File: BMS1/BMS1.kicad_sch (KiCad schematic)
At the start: 54 parts, among them J1 Conn_01x02, J2 Conn_01x02, J3 Conn_01x02, Q2 DXT5551P5-13_DIO, Q3 DXT5551P5-13_DIO, T1 ESMIT-4180_C, U1 ADG728, U10 LTC6812-1, U2 ADG728, U3 ADG728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

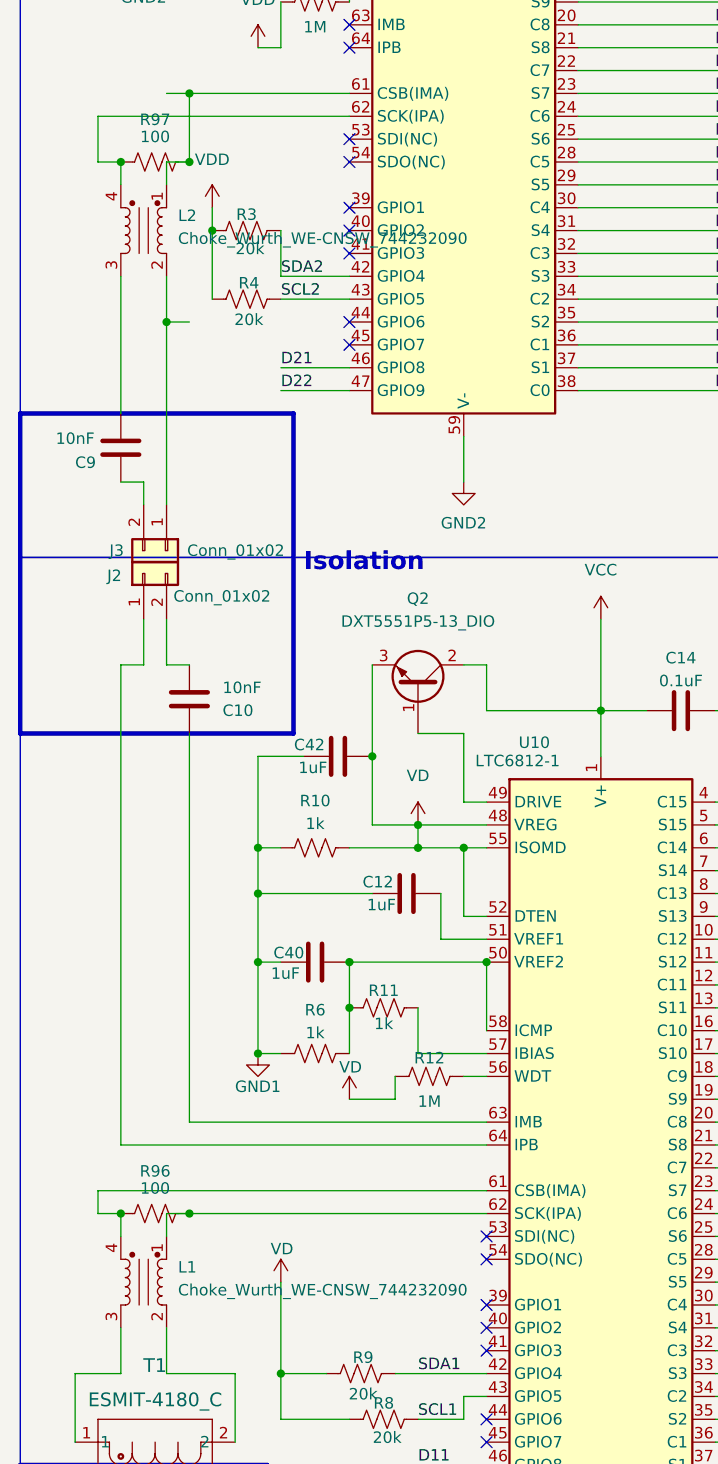
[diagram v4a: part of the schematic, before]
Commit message: updated choke symbol and footprint
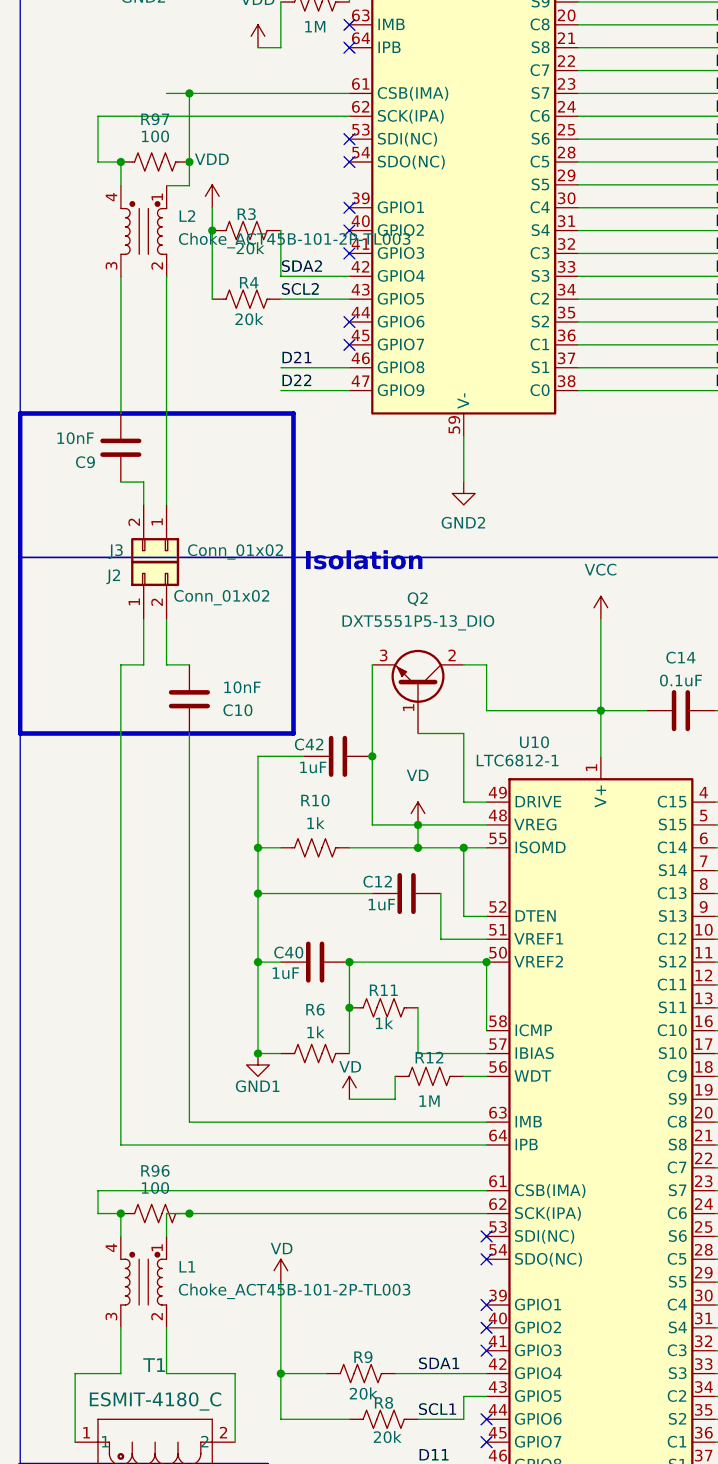
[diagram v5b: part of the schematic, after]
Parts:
- L1, L2: value Choke_Wurth_WE-CNSW_744232090 -> Choke_ACT45B-101-2P-TL003; footprint Inductor_SMD:L_CommonMode_Wurth_WE-CNSW-1206 -> AERO_Footprints:ACT45B-101-2P-TL003_TDK_new
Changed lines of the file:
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@@
 	)
 	(junction
-		(at 27.94 88.9)
-		(diameter 0)
-		(color 0 0 0 0)
-	)
-	(junction
 		(at 60.96 165.1)
 		(diameter 0)
@@
 	)
 	(junction
-		(at 33.02 106.68)
+		(at 68.58 177.8)
 		(diameter 0)
 		(color 0 0 0 0)
 	)
 	(junction
-		(at 68.58 177.8)
+		(at 231.14 43.18)
 		(diameter 0)
 		(color 0 0 0 0)
 	)
 	(junction
-		(at 231.14 43.18)
+		(at 27.94 88.9)
 		(diameter 0)
 		(color 0 0 0 0)
@@
 	(wire
 		(pts
-			(xy 33.02 101.6) (xy 33.02 106.68)
+			(xy 27.9516 116.84) (xy 27.94 116.84)
 		)
 		(stroke
@@
 	(wire
 		(pts
+			(xy 33.02 127) (xy 33.02 101.6945)
+		)
+		(stroke
+			(width 0)
+			(type default)
+		)
+	)
+	(wire
+		(pts
 			(xy 33.02 205.74) (xy 35.56 205.74)
 		)
@@
 	(wire
 		(pts
+			(xy 35.56 91.5345) (xy 33.0316 91.5345)
+		)
+		(stroke
+			(width 0)
+			(type default)
+		)
+	)
+	(wire
+		(pts
 			(xy 53.34 182.88) (xy 53.34 187.96)
 		)
@@
 		)
 	)
-	(wire
-		(pts
-			(xy 33.02 106.68) (xy 33.02 127)
-		)
-		(stroke
-			(width 0)
-			(type default)
-		)
-	)
 	(bus
 		(pts
@@
 	(wire
 		(pts
-			(xy 27.94 101.6) (xy 27.94 116.84)
-		)
-		(stroke
-			(width 0)
-			(type default)
-		)
-	)
-	(wire
-		(pts
 			(xy 27.94 198.12) (xy 68.58 198.12)
 		)
@@
 	(wire
 		(pts
-			(xy 226.06 167.64) (xy 226.06 170.18)
+			(xy 27.94 88.9) (xy 27.9516 88.9)
 		)
 		(stroke
@@
 	(wire
 		(pts
-			(xy 78.74 111.76) (xy 106.68 111.76)
+			(xy 226.06 167.64) (xy 226.06 170.18)
 		)
 		(stroke
@@
 	(wire
 		(pts
-			(xy 269.24 238.76) (xy 274.32 238.76)
+			(xy 78.74 111.76) (xy 106.68 111.76)
 		)
 		(stroke
@@
 	(wire
 		(pts
-			(xy 43.18 170.18) (xy 43.18 177.8)
+			(xy 269.24 238.76) (xy 274.32 238.76)
 		)
 		(stroke
@@
 	(wire
 		(pts
-			(xy 93.98 172.72) (xy 124.46 172.72)
+			(xy 43.18 170.18) (xy 43.18 177.8)
 		)
 		(stroke
@@
 	(wire
 		(pts
-			(xy 294.64 187.96) (xy 299.72 187.96)
+			(xy 93.98 172.72) (xy 124.46 172.72)
 		)
 		(stroke
@@
 	(wire
 		(pts
-			(xy 241.3 213.36) (xy 241.3 210.82)
+			(xy 294.64 187.96) (xy 299.72 187.96)
 		)
 		(stroke
@@
 	(wire
 		(pts
-			(xy 68.58 144.78) (xy 68.58 149.86)
+			(xy 241.3 213.36) (xy 241.3 210.82)
 		)
 		(stroke
@@
 	(wire
 		(pts
-			(xy 33.02 88.9) (xy 35.56 88.9)
+			(xy 68.58 144.78) (xy 68.58 149.86)
 		)
 		(stroke
@@
 	(wire
 		(pts
+			(xy 35.56 88.9) (xy 35.56 91.5345)
+		)
+		(stroke
+			(width 0)
+			(type default)
+		)
+	)
+	(wire
+		(pts
 			(xy 261.62 35.56) (xy 261.62 45.72)
 		)
@@
 	(wire
 		(pts
+			(xy 27.9516 101.6945) (xy 27.9516 116.84)
+		)
+		(stroke
+			(width 0)
+			(type default)
+		)
+	)
+	(wire
+		(pts
 			(xy 226.06 162.56) (xy 231.14 162.56)
 		)
@@
 	(wire
 		(pts
+			(xy 27.9516 88.9) (xy 27.9516 91.5345)
+		)
+		(stroke
+			(width 0)
+			(type default)
+		)
+	)
+	(wire
+		(pts
 			(xy 213.36 220.98) (xy 213.36 223.52)
 		)
@@
 		)
 	)
-	(wire
-		(pts
-			(xy 27.94 91.44) (xy 27.94 88.9)
-		)
-		(stroke
-			(width 0)
-			(type default)
-		)
-	)
 	(bus
 		(pts
@@
 	(wire
 		(pts
-			(xy 33.02 91.44) (xy 33.02 88.9)
+			(xy 33.02 101.6945) (xy 33.0316 101.6945)
 		)
 		(stroke
@@
 	(wire
 		(pts
-			(xy 33.02 106.68) (xy 35.56 106.68)
-		)
-		(stroke
-			(width 0)
-			(type default)
-		)
-	)
-	(wire
-		(pts
 			(xy 223.52 185.42) (xy 231.14 185.42)
 		)
@@
 	)
 	(symbol
+		(lib_name "Choke_Wurth_WE-CNSW_744232090_1")
+		(lib_id "Filter:Choke_Wurth_WE-CNSW_744232090")
+		(at 30.4916 96.6145 270)
+		(unit 1)
+		(exclude_from_sim no)
+		(in_bom yes)
+		(on_board yes)
+		(dnp no)
+		(fields_autoplaced yes)
+		(property "Reference" "L2"
+			(at 34.3016 94.9634 90)
+			(effects
+				(font
+					(size 1.27 1.27)
+				)
+				(justify left)
+			)
+		)
+		(property "Value" "Choke_ACT45B-101-2P-TL003"
+			(at 34.3016 97.5034 90)
+			(effects
+				(font
+					(size 1.27 1.27)
+				)
+				(justify left)
+			)
+		)
+		(property "Footprint" "AERO_Footprints:ACT45B-101-2P-TL003_TDK_new"
+			(at 20.3316 96.6145 0)
+			(effects
+				(font
+					(size 1.27 1.27)
+				)
+				(hide yes)
+			)
+		)
+		(property "Datasheet" "https://www.we-online.com/components/products/datasheet/744232090.pdf"
+			(at 22.8716 96.6145 0)
+			(effects
+				(font
+					(size 1.27 1.27)
+				)
+				(hide yes)
+			)
+		)
+		(property "Description" "CMC 100UH 150MA 2LN 5.8KOHM SMD"
+			(at 30.4916 96.6145 0)
+			(effects
+				(font
+					(size 1.27 1.27)
+				)
+				(hide yes)
+			)
+		)
+		(property "MPN" "744232090"
+			(at 30.4916 96.6145 0)
+			(effects
+				(font
+					(size 1.27 1.27)
+				)
+				(hide yes)
+			)
+		)
+		(pin "1"
+		)
+		(pin "2"
+		)
+		(pin "3"
+		)
+		(pin "4"
+		)
+		(instances
+			(project "BMS1"
+				(path "/03933f33-7fdb-43de-9d7d-a565cad8a277"
+					(reference "L2")
+					(unit 1)
+				)
+			)
+		)
+	)
+	(symbol
 		(lib_id "power:VDD")
 		(at 93.98 27.94 0)
@@
 	)
 	(symbol
+		(lib_name "Choke_Wurth_WE-CNSW_744232090_1")
 		(lib_id "Filter:Choke_Wurth_WE-CNSW_744232090")
 		(at 30.48 213.36 270)
@@
 			)
 		)
-		(property "Value" "Choke_Wurth_WE-CNSW_744232090"
+		(property "Value" "Choke_ACT45B-101-2P-TL003"
 			(at 34.29 214.2489 90)
 			(effects
@@
 			)
 		)
-		(property "Footprint" "Inductor_SMD:L_CommonMode_Wurth_WE-CNSW-1206"
+		(property "Footprint" "AERO_Footprints:ACT45B-101-2P-TL003_TDK_new"
 			(at 20.32 213.36 0)
 			(effects
@@
 			)
 		)
-		(property "Description" "Common mode choke, 370 mA, 125VDC, USB2.0, 111 nH"
+		(property "Description" "CMC 100UH 150MA 2LN 5.8KOHM SMD"
 			(at 30.48 213.36 0)
 			(effects
@@
 					(unit 1)
 				)
-			)
-		)
-	)
-	(symbol
-		(lib_id "Filter:Choke_Wurth_WE-CNSW_744232090")
-		(at 30.48 96.52 270)
-		(unit 1)
-		(exclude_from_sim no)
-		(in_bom yes)
-		(on_board yes)
-		(dnp no)
-		(fields_autoplaced yes)
-		(property "Reference" "L2"
-			(at 34.29 94.8689 90)
-			(effects
-				(font
-					(size 1.27 1.27)
-				)
-				(justify left)
-			)
-		)
-		(property "Value" "Choke_Wurth_WE-CNSW_744232090"
-			(at 34.29 97.4089 90)
-			(effects
-				(font
-					(size 1.27 1.27)
-				)
-				(justify left)
-			)
-		)
-		(property "Footprint" "Inductor_SMD:L_CommonMode_Wurth_WE-CNSW-1206"
-			(at 20.32 96.52 0)
-			(effects
-				(font
-					(size 1.27 1.27)
-				)
-				(hide yes)
-			)
-		)
-		(property "Datasheet" "https://www.we-online.com/components/products/datasheet/744232090.pdf"
-			(at 22.86 96.52 0)
-			(effects
-				(font
-					(size 1.27 1.27)
-				)
-				(hide yes)
-			)
-		)
-		(property "Description" "Common mode choke, 370 mA, 125VDC, USB2.0, 111 nH"
-			(at 30.48 96.52 0)
-			(effects
-				(font
-					(size 1.27 1.27)
-				)
-				(hide yes)
-			)
-		)
-		(property "MPN" "744232090"
-			(at 30.48 96.52 0)
-			(effects
-				(font
-					(size 1.27 1.27)
-				)
-				(hide yes)
-			)
-		)
-		(pin "1"
-		)
-		(pin "2"
-		)
-		(pin "3"
-		)
-		(pin "4"
-		)
-		(instances
-			(project "BMS1"
-				(path "/03933f33-7fdb-43de-9d7d-a565cad8a277"
-					(reference "L2")
-					(unit 1)
-				)

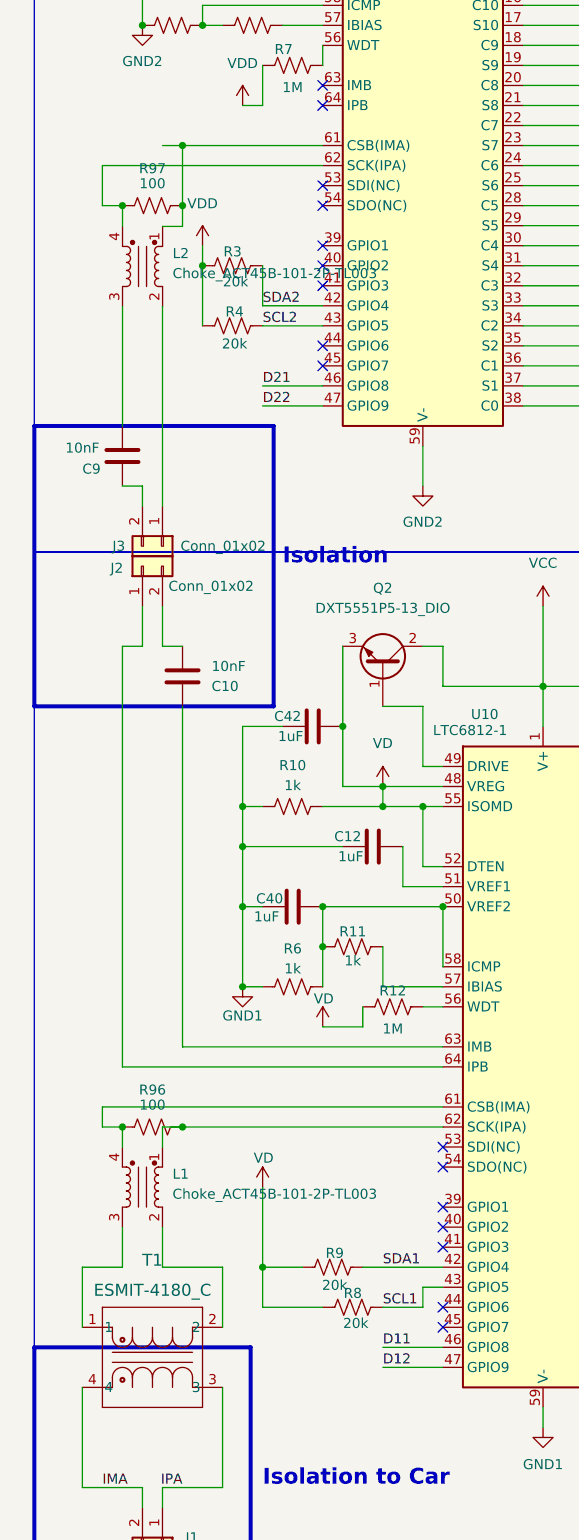
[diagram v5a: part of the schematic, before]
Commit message: rotated chokes and added datasheet info, changed a couple footprints
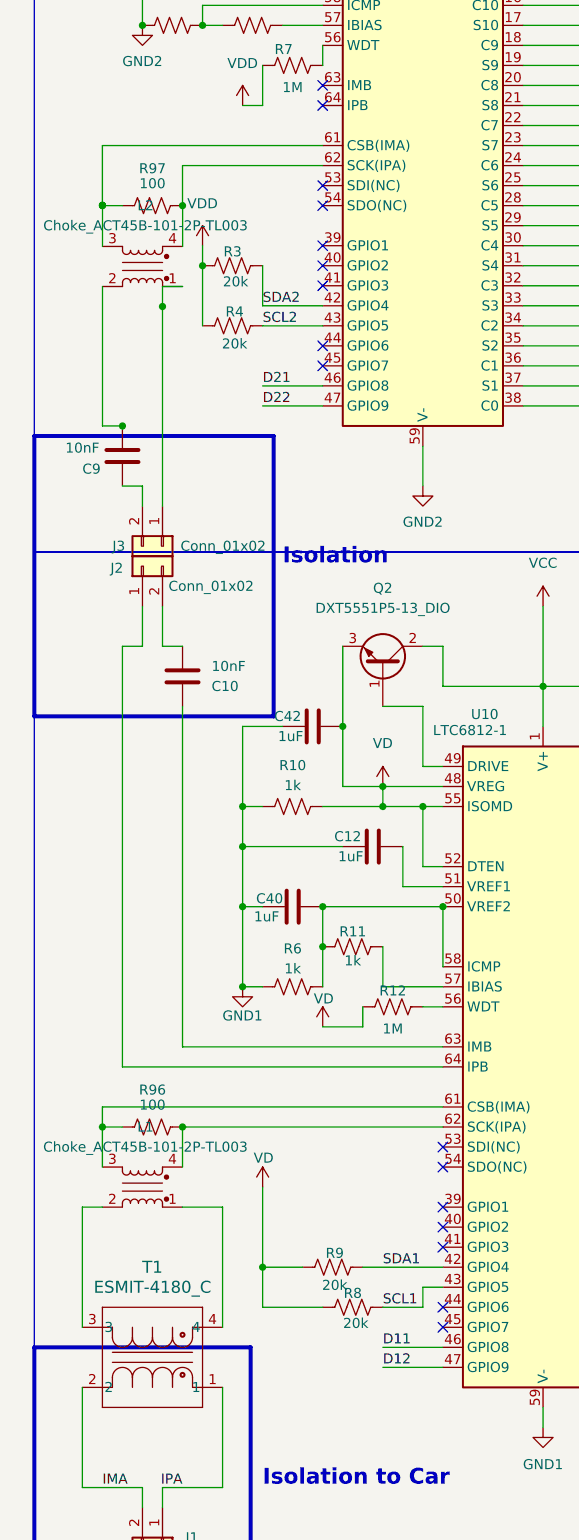
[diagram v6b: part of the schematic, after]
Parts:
- L1, L2: MPN 744232090 -> ACT45B-101-2P-TL003
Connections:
- net IMA: now also T1.2; no longer T1.4
- net IPA: now also T1.1; no longer T1.3
- net at C9.1: now also L2.2; no longer L2.3
- net at R96.2, U10.62 (SCK(IPA)): now also L1.4; no longer L1.1
- net at J3.1 (Pin_1): now also L2.1; no longer L2.2
- net at L2.4, U9.62 (SCK(IPA)): now also R97.2; no longer R97.1
- net at L1.2: now also T1.3; no longer T1.2
- net at L1.3: now also U10.61 (CSB(IMA)); no longer T1.1
- new net: L2.3, R97.1, U9.61 (CSB(IMA))
- new net: L1.1, T1.4
- now unconnected: R96.1
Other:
- moved on the sheet: L1, L2, T1

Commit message: resaved
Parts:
- R96, R97: footprint (none) -> Resistor_SMD:R_0805_2012Metric
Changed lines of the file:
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@@
 			)
 		)
-		(property "Footprint" ""
+		(property "Footprint" "Resistor_SMD:R_0805_2012Metric"
 			(at 32.004 204.724 90)
 			(effects
@@
 			)
 		)
-		(property "Footprint" ""
+		(property "Footprint" "Resistor_SMD:R_0805_2012Metric"
 			(at 32.004 87.884 90)
 			(effects

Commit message: updated datasheets and MPNs
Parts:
- D1, D2: MPN (none) -> LED WHITE DIFFUSED 2SMD
- R96, R97: MPN (none) -> CSP0603AN101-WP30300563001-3T
- T1: MPN (none) -> ESMIT-4180/C
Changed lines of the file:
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@@
 			)
 		)
-		(property "Datasheet" "~"
+		(property "Datasheet" "https://mm.digikey.com/Volume0/opasdata/d220001/medias/docus/4310/CSP0603AN101-WP30300563001-3T_V6_2-26-21.pdf"
 			(at 31.75 205.74 0)
 			(effects
@@
 			)
 		)
-		(property "MPN" ""
+		(property "MPN" "CSP0603AN101-WP30300563001-3T"
 			(at 31.75 205.74 0)
 			(effects
@@
 			)
 		)
-		(property "Datasheet" "~"
+		(property "Datasheet" "https://mm.digikey.com/Volume0/opasdata/d220001/medias/docus/4310/CSP0603AN101-WP30300563001-3T_V6_2-26-21.pdf"
 			(at 107.95 142.24 0)
 			(effects
@@
 			)
 		)
-		(property "MPN" ""
+		(property "MPN" "LED WHITE DIFFUSED 2SMD"
 			(at 107.95 142.24 0)
 			(effects
@@
 			)
 		)
-		(property "Datasheet" "~"
+		(property "Datasheet" "https://mm.digikey.com/Volume0/opasdata/d220001/medias/docus/4310/CSP0603AN101-WP30300563001-3T_V6_2-26-21.pdf"
 			(at 31.75 88.9 0)
 			(effects
@@
 			)
 		)
-		(property "MPN" ""
+		(property "MPN" "CSP0603AN101-WP30300563001-3T"
 			(at 31.75 88.9 0)
 			(effects
@@
 			)
 		)
-		(property "Datasheet" "~"
+		(property "Datasheet" "https://mm.digikey.com/Volume0/opasdata/d220001/medias/docus/4310/CSP0603AN101-WP30300563001-3T_V6_2-26-21.pdf"
 			(at 105.41 27.94 0)
 			(effects
@@
 			)
 		)
-		(property "MPN" ""
+		(property "MPN" "LED WHITE DIFFUSED 2SMD"
 			(at 105.41 27.94 0)
 			(effects
@@
 			)
 		)
-		(property "Datasheet" "ESMIT-4180/C"
+		(property "Datasheet" "https://products.sumida.com/products/pdf/CBM5D33_Ver1.0_E.pdf"
 			(at 40.64 238.76 0)
 			(effects
@@
 			)
 		)
-		(property "MPN" ""
+		(property "MPN" "ESMIT-4180/C"
 			(at 40.64 238.76 0)
 			(effects
